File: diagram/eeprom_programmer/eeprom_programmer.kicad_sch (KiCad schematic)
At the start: 2 parts

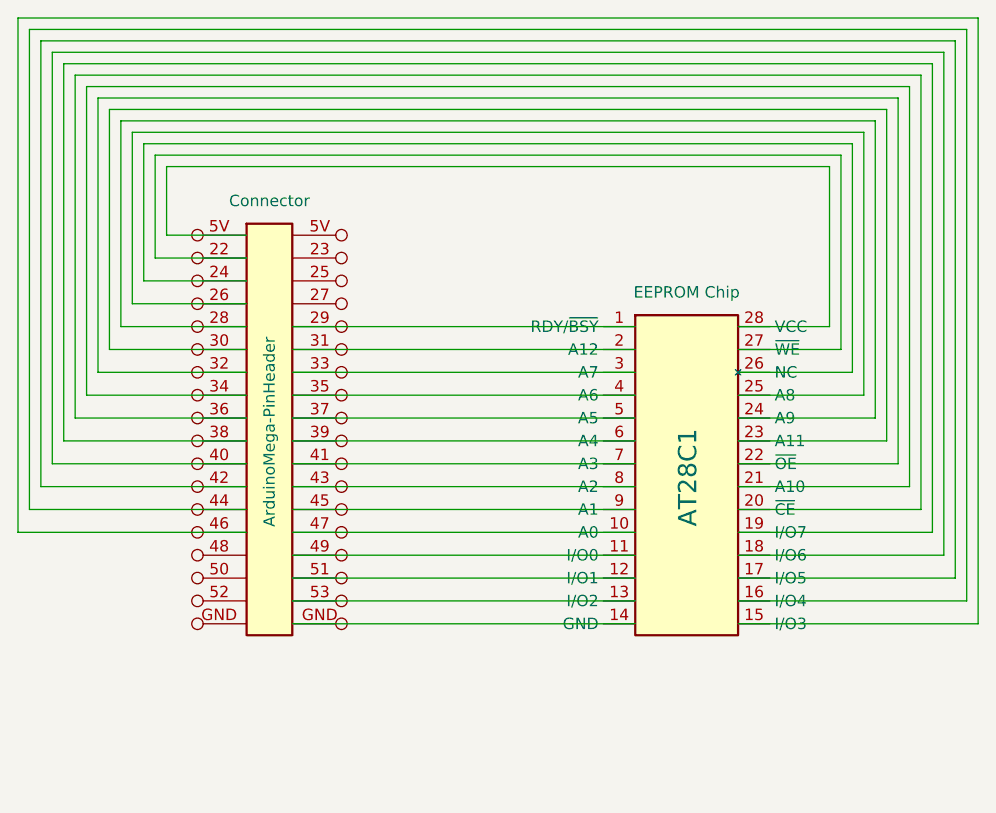
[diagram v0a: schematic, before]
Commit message: update wiring diagram
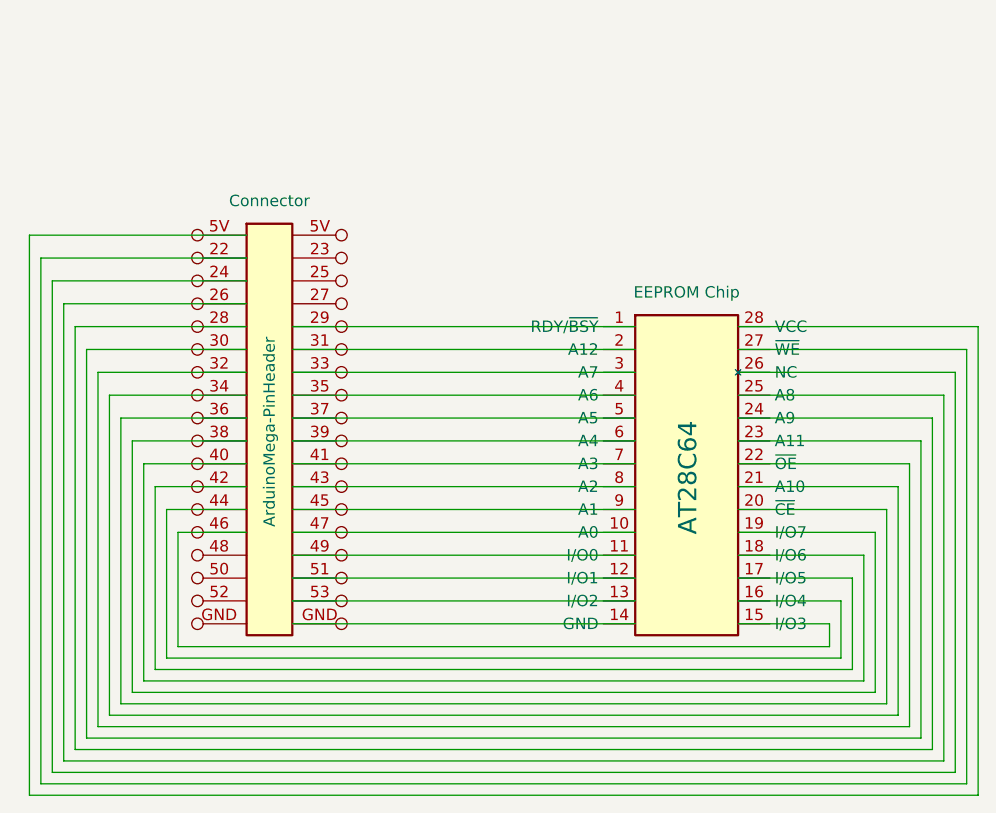
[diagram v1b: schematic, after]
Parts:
- renumbered AT28C1 to AT28C64
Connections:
- net at ArduinoMega-PinHeader.5V: now also AT28C64.28 (VCC)
- net at ArduinoMega-PinHeader.GND: now also AT28C64.14 (GND)

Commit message: update wiring diagram
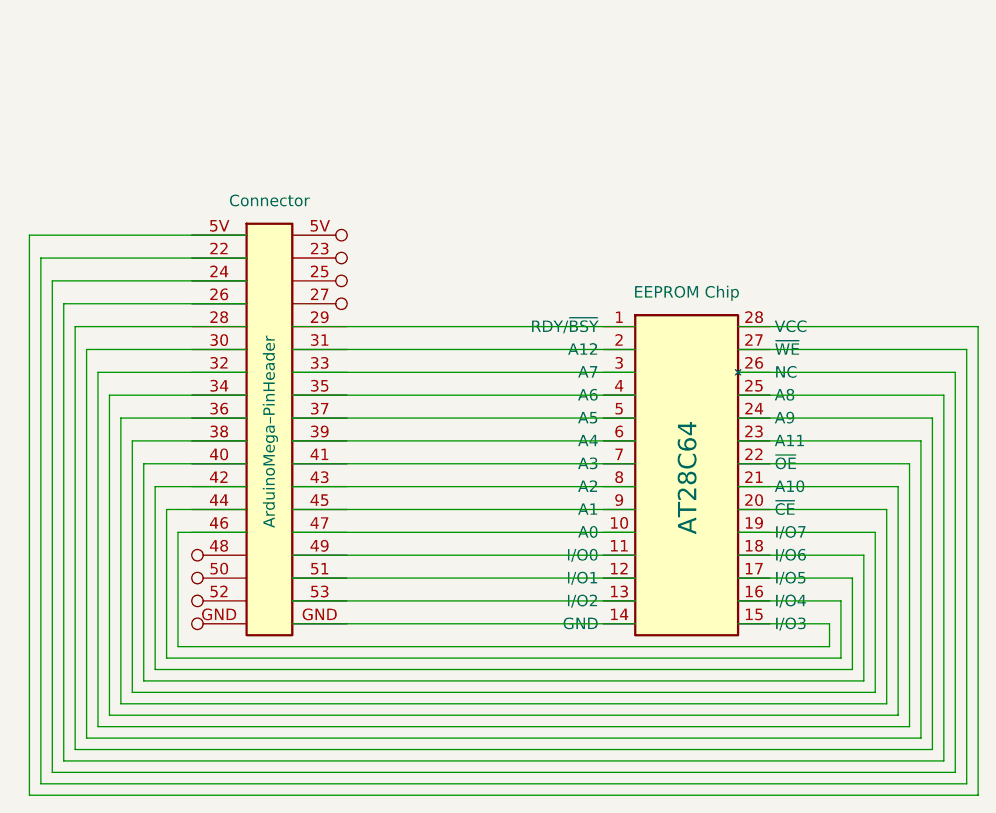
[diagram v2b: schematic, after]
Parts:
- removed ArduinoMega-PinHeader: Connector, symbol MCU_Module:Arduino_Mega_2560_PinHeader
- added ArduinoMega–PinHeader: Connector, symbol MCU_Module:Arduino_Mega_2560_PinHeader_Conn
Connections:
- net at AT28C64.27 (~{WE}): now also ArduinoMega–PinHeader.22
- net at AT28C64.26 (NC): now also ArduinoMega–PinHeader.24
- net at AT28C64.25 (A8): now also ArduinoMega–PinHeader.26
- net at AT28C64.24 (A9): now also ArduinoMega–PinHeader.28
- net at AT28C64.1 (RDY/~{BSY}): now also ArduinoMega–PinHeader.29
- net at AT28C64.23 (A11): now also ArduinoMega–PinHeader.30
- net at AT28C64.2 (A12): now also ArduinoMega–PinHeader.31
- net at AT28C64.22 (~{OE}): now also ArduinoMega–PinHeader.32
- net at AT28C64.3 (A7): now also ArduinoMega–PinHeader.33
- net at AT28C64.21 (A10): now also ArduinoMega–PinHeader.34
- net at AT28C64.4 (A6): now also ArduinoMega–PinHeader.35
- net at AT28C64.20 (~{CE}): now also ArduinoMega–PinHeader.36
- net at AT28C64.5 (A5): now also ArduinoMega–PinHeader.37
- net at AT28C64.19 (I/O7): now also ArduinoMega–PinHeader.38
- net at AT28C64.6 (A4): now also ArduinoMega–PinHeader.39
- net at AT28C64.18 (I/O6): now also ArduinoMega–PinHeader.40
- net at AT28C64.7 (A3): now also ArduinoMega–PinHeader.41
- net at AT28C64.17 (I/O5): now also ArduinoMega–PinHeader.42
- net at AT28C64.8 (A2): now also ArduinoMega–PinHeader.43
- net at AT28C64.16 (I/O4): now also ArduinoMega–PinHeader.44
- net at AT28C64.9 (A1): now also ArduinoMega–PinHeader.45
- net at AT28C64.15 (I/O3): now also ArduinoMega–PinHeader.46
- net at AT28C64.10 (A0): now also ArduinoMega–PinHeader.47
- net at AT28C64.11 (I/O0): now also ArduinoMega–PinHeader.49
- net at AT28C64.12 (I/O1): now also ArduinoMega–PinHeader.51
- net at AT28C64.13 (I/O2): now also ArduinoMega–PinHeader.53
- net at AT28C64.28 (VCC): now also ArduinoMega–PinHeader.5V
- net at AT28C64.14 (GND): now also ArduinoMega–PinHeader.GND
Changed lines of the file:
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@@
-	)
-	(symbol
-		(lib_id "MCU_Module:Arduino_Mega_2560_PinHeader")
-		(at 99.06 67.31 0)
-		(unit 1)
-		(exclude_from_sim no)
-		(in_bom yes)
-		(on_board yes)
-		(dnp no)
-		(fields_autoplaced yes)
-		(property "Reference" "ArduinoMega-PinHeader"
-			(at 99.06 67.564 90)
-			(do_not_autoplace yes)
-			(effects
-				(font
-					(size 1.27 1.27)
-				)
-			)
-		)
-		(property "Value" "Connector"
-			(at 99.06 41.91 0)
-			(effects
-				(font
-					(size 1.27 1.27)
-				)
-			)
-		)
-		(property "Footprint" ""
-			(at 99.06 67.31 0)
-			(effects
-				(font
-					(size 1.27 1.27)
-				)
-				(hide yes)
-			)
-		)
-		(property "Datasheet" ""
-			(at 99.06 67.31 0)
-			(effects
-				(font
-					(size 1.27 1.27)
-				)
-				(hide yes)
-			)
-		)
-		(property "Description" ""
-			(at 99.06 67.31 0)
-			(effects
-				(font
-					(size 1.27 1.27)
-				)
-				(hide yes)
-			)
-		)
-		(pin "34"
-		)
-		(pin "52"
-		)
-		(pin "50"
-		)
-		(pin "48"
-		)
-		(pin "28"
-		)
-		(pin "30"
-		)
-		(pin "26"
-		)
-		(pin "51"
-		)
-		(pin "22"
-		)
-		(pin "5V"
-		)
-		(pin "37"
-		)
-		(pin "GND"
-		)
-		(pin "24"
-		)
-		(pin "49"
-		)
-		(pin "44"
-		)
-		(pin "42"
-		)
-		(pin "39"
-		)
-		(pin "5V"
-		)
-		(pin "25"
-		)
-		(pin "33"
-		)
-		(pin "31"
-		)
-		(pin "27"
-		)
-		(pin "29"
-		)
-		(pin "23"
-		)
-		(pin "46"
-		)
-		(pin "43"
-		)
-		(pin "41"
-		)
-		(pin "35"
-		)
-		(pin "53"
-		)
-		(pin "36"
-		)
-		(pin "40"
-		)
-		(pin "38"
-		)
-		(pin "GND"
-		)
-		(pin "32"
-		)
-		(pin "45"
-		)
-		(pin "47"
-		)
-		(instances
-			(project ""
-				(path "/758b2bf2-b8e4-4334-80c5-ff5056cbce48"
-					(reference "ArduinoMega-PinHeader")
-					(unit 1)
-				)
-			)
-		)
 	)
 	(symbol
@@
 					(unit 1)
 				)
+			)
+		)
+	)
+	(symbol
+		(lib_id "MCU_Module:Arduino_Mega_2560_PinHeader_Conn")
+		(at 99.06 67.31 0)
+		(unit 1)
+		(exclude_from_sim no)
+		(in_bom yes)
+		(on_board yes)
+		(dnp no)
+		(fields_autoplaced yes)
+		(property "Reference" "ArduinoMega–PinHeader"
+			(at 99.06 67.564 90)
+			(do_not_autoplace yes)
+			(effects
+				(font
+					(size 1.27 1.27)
+				)
+			)
+		)
+		(property "Value" "Connector"
+			(at 99.06 41.91 0)
+			(effects
+				(font
+					(size 1.27 1.27)
+				)
+			)
+		)
+		(property "Footprint" ""
+			(at 99.06 67.31 0)
+			(effects
+				(font
+					(size 1.27 1.27)
+				)
+				(hide yes)
+			)
+		)
+		(property "Datasheet" ""
+			(at 99.06 67.31 0)
+			(effects
+				(font
+					(size 1.27 1.27)
+				)
+				(hide yes)
+			)
+		)
+		(property "Description" ""
+			(at 99.06 67.31 0)
+			(effects
+				(font
+					(size 1.27 1.27)
+				)
+				(hide yes)
+			)
+		)
+		(pin "46"
+		)
+		(pin "48"
+		)
+		(pin "42"
+		)
+		(pin "44"
+		)
+		(pin "52"
+		)
+		(pin "39"
+		)
+		(pin "22"
+		)
+		(pin "5V"
+		)
+		(pin "45"
+		)
+		(pin "51"
+		)
+		(pin "31"
+		)
+		(pin "40"
+		)
+		(pin "5V"
+		)
+		(pin "GND"
+		)
+		(pin "GND"
+		)
+		(pin "23"
+		)
+		(pin "27"
+		)
+		(pin "43"
+		)
+		(pin "35"
+		)
+		(pin "33"
+		)
+		(pin "50"
+		)
+		(pin "25"
+		)
+		(pin "29"
+		)
+		(pin "53"
+		)
+		(pin "49"
+		)
+		(pin "38"
+		)
+		(pin "30"
+		)
+		(pin "34"
+		)
+		(pin "28"
+		)
+		(pin "36"
+		)
+		(pin "26"
+		)
+		(pin "32"
+		)
+		(pin "24"
+		)
+		(pin "47"
+		)
+		(pin "37"
+		)
+		(pin "41"
+		)
+		(instances
+			(project ""
+				(path "/758b2bf2-b8e4-4334-80c5-ff5056cbce48"
+					(reference "ArduinoMega–PinHeader")
+					(unit 1)
+				)

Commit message: update wiring diagram
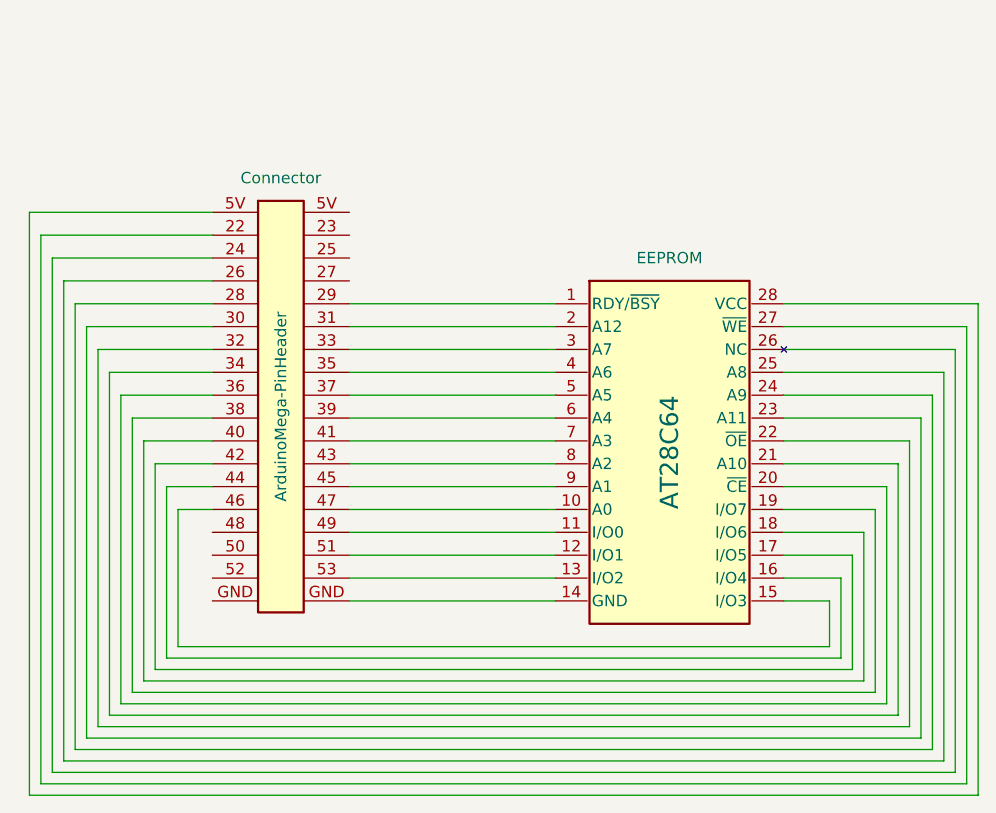
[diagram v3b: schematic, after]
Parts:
- removed ArduinoMega–PinHeader: Connector, symbol MCU_Module:Arduino_Mega_2560_PinHeader_Conn
- added ArduinoMega-PinHeader: Connector, symbol MCU_Module:Arduino_Mega_2560_PinHeader
- AT28C64: value EEPROM Chip -> EEPROM
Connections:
- net at AT28C64.1 (RDY/~{BSY}): now also ArduinoMega-PinHeader.29
- net at AT28C64.10 (A0): now also ArduinoMega-PinHeader.47
- net at AT28C64.11 (I/O0): now also ArduinoMega-PinHeader.49
- net at AT28C64.12 (I/O1): now also ArduinoMega-PinHeader.51
- net at AT28C64.13 (I/O2): now also ArduinoMega-PinHeader.53
- net at AT28C64.14 (GND): now also ArduinoMega-PinHeader.GND
- net at AT28C64.15 (I/O3): now also ArduinoMega-PinHeader.46
- net at AT28C64.16 (I/O4): now also ArduinoMega-PinHeader.44
- net at AT28C64.17 (I/O5): now also ArduinoMega-PinHeader.42
- net at AT28C64.18 (I/O6): now also ArduinoMega-PinHeader.40
- net at AT28C64.19 (I/O7): now also ArduinoMega-PinHeader.38
- net at AT28C64.2 (A12): now also ArduinoMega-PinHeader.31
- net at AT28C64.20 (~{CE}): now also ArduinoMega-PinHeader.36
- net at AT28C64.21 (A10): now also ArduinoMega-PinHeader.34
- net at AT28C64.22 (~{OE}): now also ArduinoMega-PinHeader.32
- net at AT28C64.23 (A11): now also ArduinoMega-PinHeader.30
- net at AT28C64.24 (A9): now also ArduinoMega-PinHeader.28
- net at AT28C64.25 (A8): now also ArduinoMega-PinHeader.26
- net at AT28C64.26 (NC): now also ArduinoMega-PinHeader.24
- net at AT28C64.27 (~{WE}): now also ArduinoMega-PinHeader.22
- net at AT28C64.28 (VCC): now also ArduinoMega-PinHeader.5V
- net at AT28C64.3 (A7): now also ArduinoMega-PinHeader.33
- net at AT28C64.4 (A6): now also ArduinoMega-PinHeader.35
- net at AT28C64.5 (A5): now also ArduinoMega-PinHeader.37
- net at AT28C64.6 (A4): now also ArduinoMega-PinHeader.39
- net at AT28C64.7 (A3): now also ArduinoMega-PinHeader.41
- net at AT28C64.8 (A2): now also ArduinoMega-PinHeader.43
- net at AT28C64.9 (A1): now also ArduinoMega-PinHeader.45

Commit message: update wiring diagram
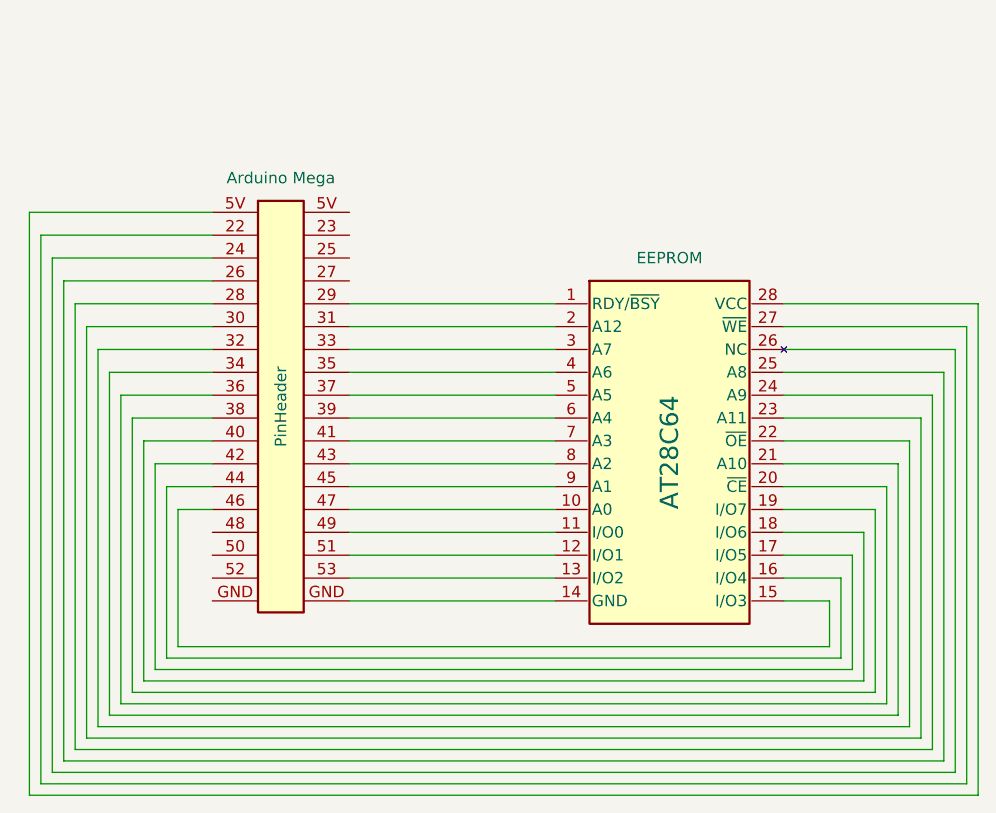
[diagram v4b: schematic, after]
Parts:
- PinHeader: renamed from ArduinoMega-PinHeader; value Connector -> Arduino Mega
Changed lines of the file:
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@@
 		(dnp no)
 		(fields_autoplaced yes)
-		(property "Reference" "ArduinoMega-PinHeader"
+		(property "Reference" "PinHeader"
 			(at 100.33 64.77 90)
 			(do_not_autoplace yes)
@@
 			)
 		)
-		(property "Value" "Connector"
+		(property "Value" "Arduino Mega"
 			(at 100.33 39.37 0)
 			(effects
@@
 			(project ""
 				(path "/758b2bf2-b8e4-4334-80c5-ff5056cbce48"
-					(reference "ArduinoMega-PinHeader")
+					(reference "PinHeader")
 					(unit 1)
 				)
